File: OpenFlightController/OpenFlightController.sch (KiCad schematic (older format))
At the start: 0 parts

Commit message: EdgeCuts PCB 0.1v
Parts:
- added U1: STM32F405RGT6, Package_SO:MAX7456, symbol STM32F405RGT6:STM32F405RGT6
- added U2: MAX7456EUI+, Package_SO:MAX7456, symbol MAX7456EUI_:MAX7456EUI+
- added U?: MPU-6000, Sensor_Motion:InvenSense_QFN-24_4x4mm_P0.5mm, symbol Sensor_Motion:MPU-6000
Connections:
- new net: U1.18 (VSS), U1.63 (VSS)
- new net: U1.19 (VDD), U1.32 (VDD), U1.48 (VDD), U1.64 (VDD)
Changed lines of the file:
@@
 Comment4 ""
 $EndDescr
+$Comp
+L STM32F405RGT6:STM32F405RGT6 U1
+U 1 1 5E3B0E09
+P 2150 3150
+F 0 "U1" H 2150 5620 50  0000 C CNN
+F 1 "STM32F405RGT6" H 2150 5529 50  0000 C CNN
+F 2 "Package_SO:MAX7456" H 2150 3150 50  0001 L BNN
+F 3 "LTR" H 2150 3150 50  0001 L BNN
+F 4 "STMicroelectronics" H 2150 3150 50  0001 L BNN "Campo4"
+F 5 "IPC-7351B" H 2150 3150 50  0001 L BNN "Campo5"
+	1    2150 3150
+	1    0    0    -1
+$EndComp
+$Comp
+L MAX7456EUI_:MAX7456EUI+ U2
+U 1 1 5E3B414B
+P 7900 2600
+F 0 "U2" H 7900 3670 50  0000 C CNN
+F 1 "MAX7456EUI+" H 7900 3579 50  0000 C CNN
+F 2 "Package_SO:MAX7456" H 7900 2600 50  0001 L BNN
+F 3 "" H 7900 2600 50  0001 C CNN
+	1    7900 2600
+	1    0    0    -1
+$EndComp
+$Comp
+L Sensor_Motion:MPU-6000 U?
+U 1 1 5E3B576F
+P 6950 5200
+F 0 "U?" H 6950 6081 50  0000 C CNN
+F 1 "MPU-6000" H 6950 5990 50  0000 C CNN
+F 2 "Sensor_Motion:InvenSense_QFN-24_4x4mm_P0.5mm" H 6950 4400 50  0001 C CNN
+F 3 "https://store.invensense.com/datasheets/invensense/MPU-6050_DataSheet_V3%204.pdf" H 6950 5050 50  0001 C CNN
+	1    6950 5200
+	1    0    0    -1
+$EndComp
 $EndSCHEMATC

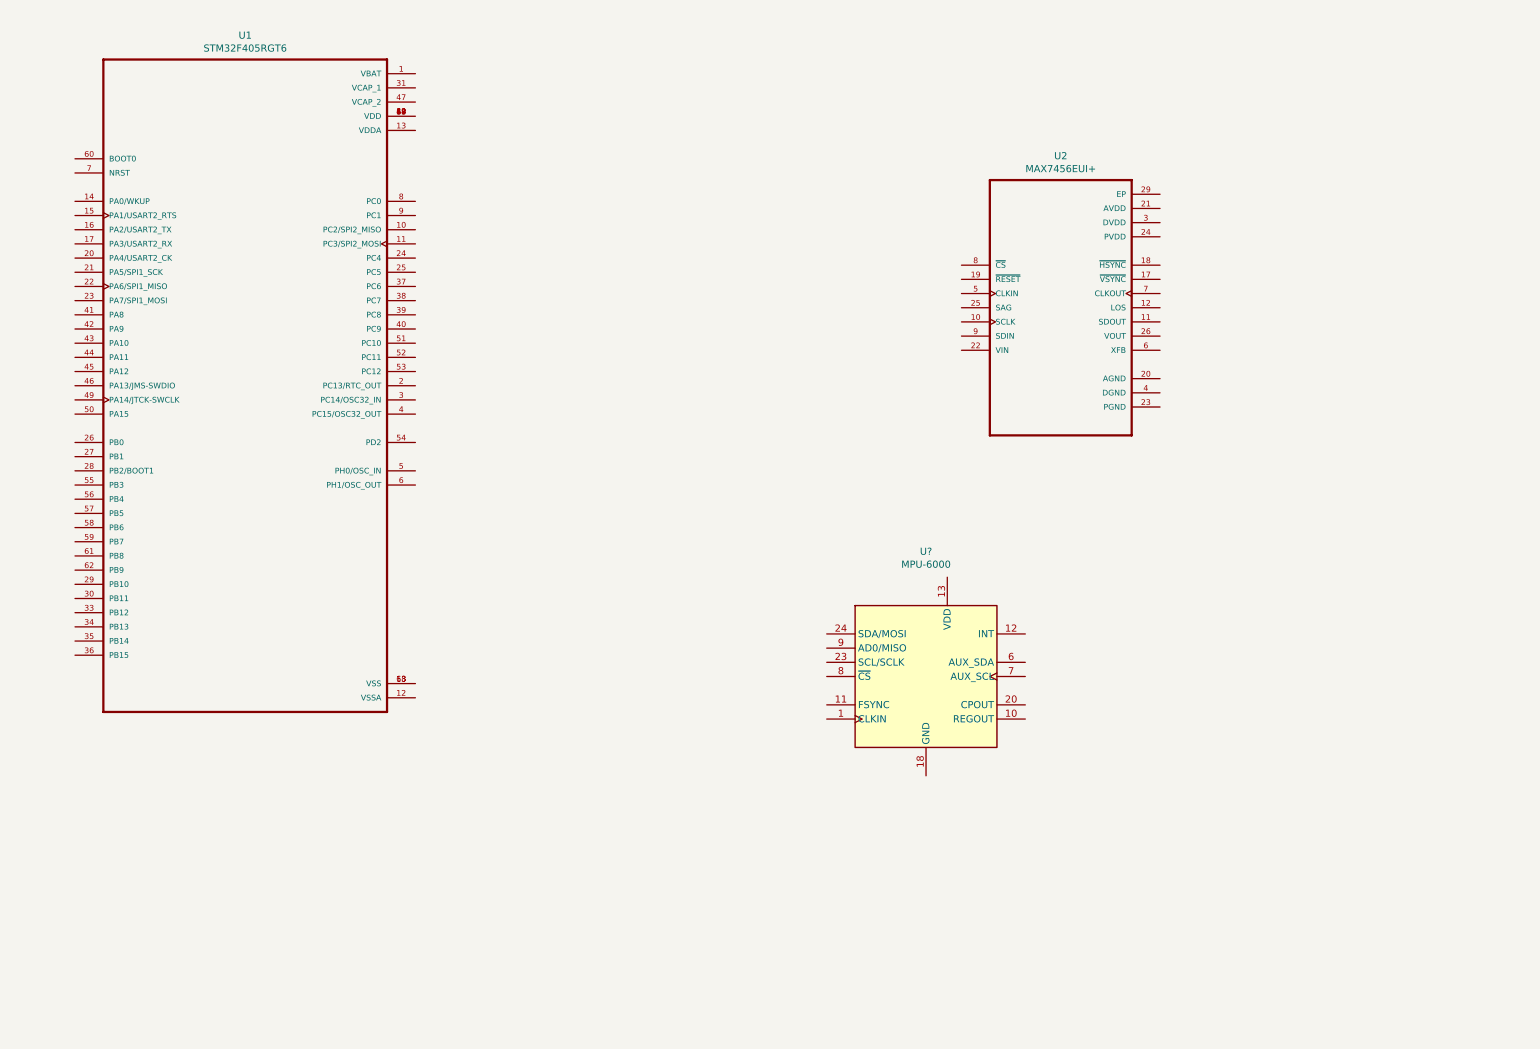
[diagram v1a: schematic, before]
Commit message: Add Power In 3v3
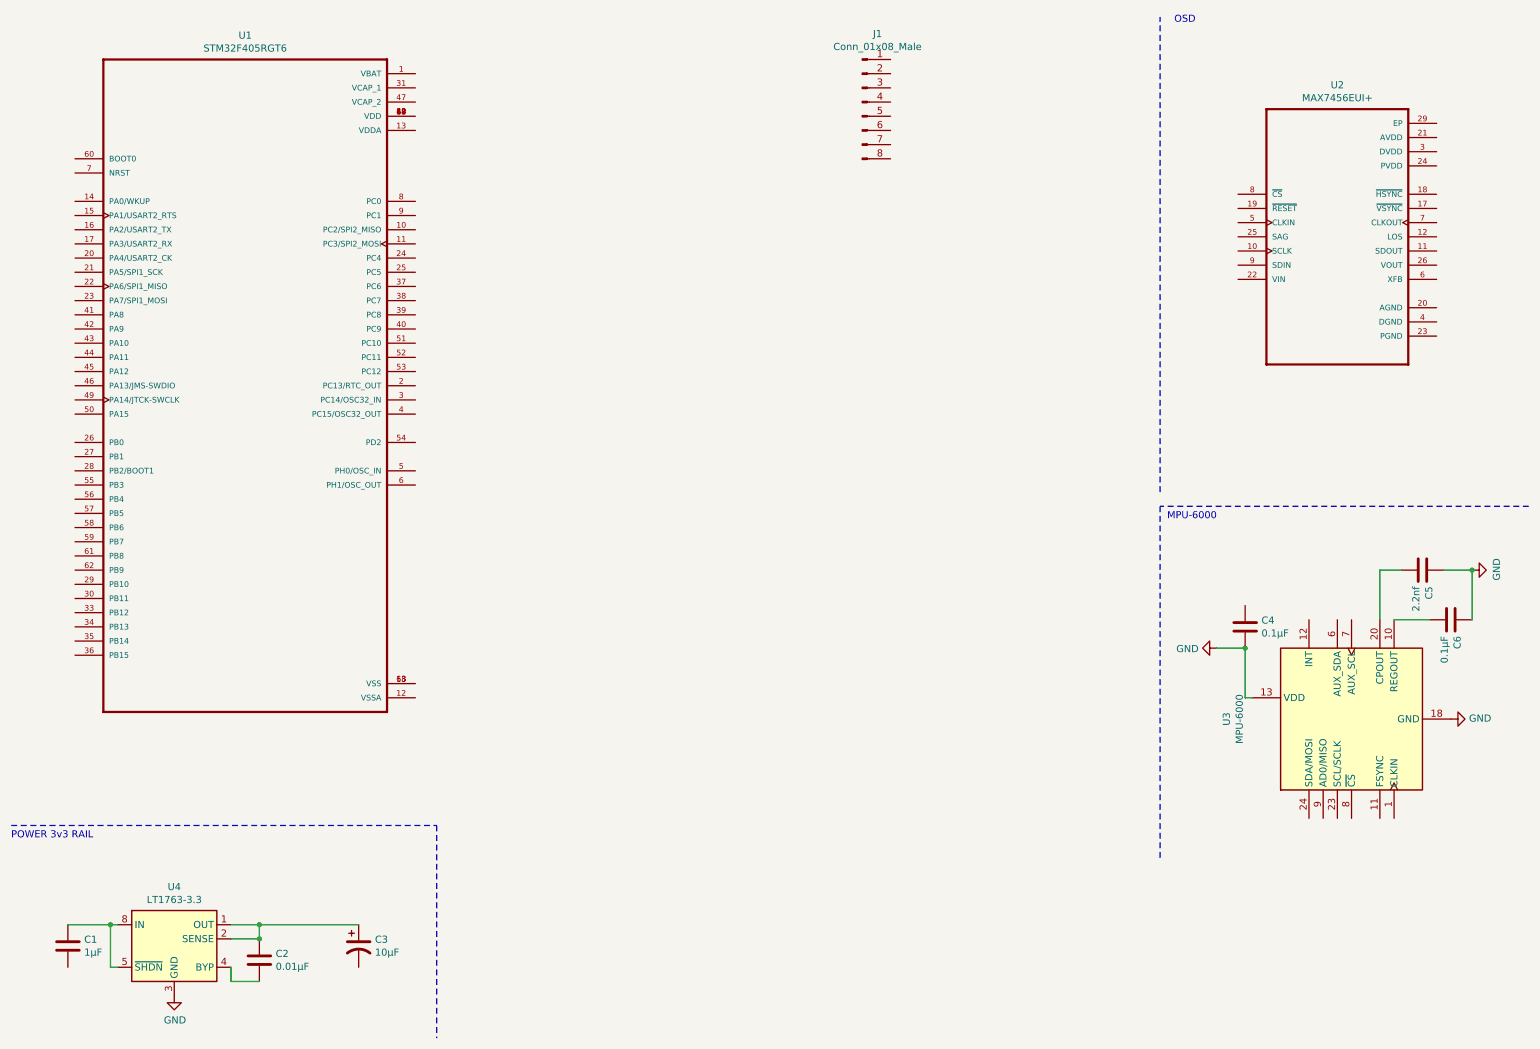
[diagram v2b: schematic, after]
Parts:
- added C1: 1µF, Capacitor_SMD:C_0603_1608Metric, symbol Device:C
- added C2: 0.01µF, Capacitor_SMD:C_0603_1608Metric, symbol Device:C
- added C3: 10µF, symbol Device:CP1
- added C4, C6: 0.1µF, Capacitor_SMD:C_0603_1608Metric, symbol Device:C
- added C5: 2.2nf, Capacitor_SMD:C_0603_1608Metric, symbol Device:C
- added J1: Conn_01x08_Male, Connector_JST:JST_GH_SM08B-GHS-TB_1x08-1MP_P1.25mm_Horizontal, symbol Connector:Conn_01x08_Male
- added U4: LT1763-3.3, Package_SO:SOP-8_3.76x4.96mm_P1.27mm, symbol Regulator_Linear:LT1763-3.3
- gave numbers to parts that had none: 1
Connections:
- net at U3.10 (REGOUT): now also C6.2
- net GND: now reaches U3.13 (VDD)
- net GND: now also U3.18 (GND), C4.2, C5.1, C6.1, U4.3 (GND)
- net at U3.20 (CPOUT): now also C5.2
- new net: C2.1, C3.1, U4.1 (OUT), U4.2 (SENSE)
- new net: C2.2, U4.4 (BYP)
- new net: C1.1, U4.5 (~SHDN), U4.8 (IN)
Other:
- note added: "MPU-6000\n"
- note added: "OSD"
- note added: "POWER 3v3 RAIL\n"
- moved on the sheet: U2, U3
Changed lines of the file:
@@
 L MAX7456EUI_:MAX7456EUI+ U2
 U 1 1 5E3B414B
-P 7900 2600
-F 0 "U2" H 7900 3670 50  0000 C CNN
-F 1 "MAX7456EUI+" H 7900 3579 50  0000 C CNN
-F 2 "Package_SO:MAX7456" H 7900 2600 50  0001 L BNN
-F 3 "" H 7900 2600 50  0001 C CNN
-	1    7900 2600
-	1    0    0    -1
-$EndComp
-$Comp
-L Sensor_Motion:MPU-6000 U?
+P 9850 2100
+F 0 "U2" H 9850 3170 50  0000 C CNN
+F 1 "MAX7456EUI+" H 9850 3079 50  0000 C CNN
+F 2 "Package_SO:MAX7456" H 9850 2100 50  0001 L BNN
+F 3 "" H 9850 2100 50  0001 C CNN
+	1    9850 2100
+	1    0    0    -1
+$EndComp
+$Comp
+L Regulator_Linear:LT1763-3.3 U4
+U 1 1 5E3E488E
+P 1650 7150
+F 0 "U4" H 1650 7617 50  0000 C CNN
+F 1 "LT1763-3.3" H 1650 7526 50  0000 C CNN
+F 2 "Package_SO:SOP-8_3.76x4.96mm_P1.27mm" H 1650 6800 50  0001 C CNN
+F 3 "https://www.analog.com/media/en/technical-documentation/data-sheets/1962fb.pdf" H 1650 6600 50  0001 C CNN
+	1    1650 7150
+	1    0    0    -1
+$EndComp
+$Comp
+L Device:C C2
+U 1 1 5E3E80B6
+P 2250 7200
+F 0 "C2" H 2365 7246 50  0000 L CNN
+F 1 "0.01µF" H 2365 7155 50  0000 L CNN
+F 2 "Capacitor_SMD:C_0603_1608Metric" H 2288 7050 50  0001 C CNN
+F 3 "~" H 2250 7200 50  0001 C CNN
+	1    2250 7200
+	1    0    0    -1
+$EndComp
+$Comp
+L Device:CP1 C3
+U 1 1 5E3E8CF6
+P 2950 7100
+F 0 "C3" H 3065 7146 50  0000 L CNN
+F 1 "10µF" H 3065 7055 50  0000 L CNN
+F 2 "" H 2950 7100 50  0001 C CNN
+F 3 "~" H 2950 7100 50  0001 C CNN
+	1    2950 7100
+	1    0    0    -1
+$EndComp
+$Comp
+L Device:C C1
+U 1 1 5E3E966D
+P 900 7100
+F 0 "C1" H 1015 7146 50  0000 L CNN
+F 1 "1µF" H 1015 7055 50  0000 L CNN
+F 2 "Capacitor_SMD:C_0603_1608Metric" H 938 6950 50  0001 C CNN
+F 3 "~" H 900 7100 50  0001 C CNN
+	1    900  7100
+	1    0    0    -1
+$EndComp
+Wire Wire Line
+	2050 7250 2050 7350
+Wire Wire Line
+	2050 7350 2250 7350
+Wire Wire Line
+	2250 7050 2250 6950
+Wire Wire Line
+	2250 6950 2050 6950
+Wire Wire Line
+	2050 7050 2250 7050
+Connection ~ 2250 7050
+Wire Wire Line
+	2250 6950 2950 6950
+Connection ~ 2250 6950
+Wire Wire Line
+	1250 7250 1200 7250
+Wire Wire Line
+	1200 7250 1200 6950
+Wire Wire Line
+	1200 6950 1250 6950
+Wire Wire Line
+	1200 6950 900  6950
+Connection ~ 1200 6950
+Wire Notes Line
+	500  6250 3500 6250
+Wire Notes Line
+	3500 6250 3500 7750
+Text Notes 500  6350 0    50   ~ 0
+POWER 3v3 RAIL\n
+$Comp
+L Device:C C5
+U 1 1 5E3EF61B
+P 10450 4450
+F 0 "C5" H 10565 4496 50  0000 L CNN
+F 1 "2.2nf" H 10565 4405 50  0000 L CNN
+F 2 "Capacitor_SMD:C_0603_1608Metric" H 10488 4300 50  0001 C CNN
+F 3 "~" H 10450 4450 50  0001 C CNN
+	1    10450 4450
+	0    1    1    0
+$EndComp
+$Comp
+L Device:C C6
+U 1 1 5E3F2D0D
+P 10650 4800
+F 0 "C6" H 10765 4846 50  0000 L CNN
+F 1 "0.1µF" H 10765 4755 50  0000 L CNN
+F 2 "Capacitor_SMD:C_0603_1608Metric" H 10688 4650 50  0001 C CNN
+F 3 "~" H 10650 4800 50  0001 C CNN
+	1    10650 4800
+	0    1    1    0
+$EndComp
+Wire Wire Line
+	9250 5350 9200 5350
+Wire Wire Line
+	9200 5350 9200 5000
+Wire Wire Line
+	9200 5000 9000 5000
+Connection ~ 9200 5000
+$Comp
+L Device:C C4
+U 1 1 5E3F0351
+P 9200 4850
+F 0 "C4" H 9315 4896 50  0000 L CNN
+F 1 "0.1µF" H 9315 4805 50  0000 L CNN
+F 2 "Capacitor_SMD:C_0603_1608Metric" H 9238 4700 50  0001 C CNN
+F 3 "~" H 9200 4850 50  0001 C CNN
+	1    9200 4850
+	1    0    0    -1
+$EndComp
+$Comp
+L Sensor_Motion:MPU-6000 U3
 U 1 1 5E3B576F
-P 6950 5200
-F 0 "U?" H 6950 6081 50  0000 C CNN
-F 1 "MPU-6000" H 6950 5990 50  0000 C CNN
-F 2 "Sensor_Motion:InvenSense_QFN-24_4x4mm_P0.5mm" H 6950 4400 50  0001 C CNN
-F 3 "https://store.invensense.com/datasheets/invensense/MPU-6050_DataSheet_V3%204.pdf" H 6950 5050 50  0001 C CNN
-	1    6950 5200
-	1    0    0    -1
-$EndComp
+P 9950 5500
+F 0 "U3" H 9950 6381 50  0000 C CNN
+F 1 "MPU-6000" H 9950 6290 50  0000 C CNN
+F 2 "Sensor_Motion:InvenSense_QFN-24_4x4mm_P0.5mm" H 9950 4700 50  0001 C CNN
+F 3 "https://store.invensense.com/datasheets/invensense/MPU-6050_DataSheet_V3%204.pdf" H 9950 5350 50  0001 C CNN
+	1    9950 5500
+	0    -1   -1   0
+$EndComp
+$Comp
+L power:GND #PWR0101
+U 1 1 5E4011D4
+P 10650 5500
+F 0 "#PWR0101" H 10650 5250 50  0001 C CNN
+F 1 "GND" V 10655 5372 50  0000 R CNN
+F 2 "" H 10650 5500 50  0001 C CNN
+F 3 "" H 10650 5500 50  0001 C CNN
+	1    10650 5500
+	0    -1   -1   0
+$EndComp
+$Comp
+L power:GND #PWR0102
+U 1 1 5E401C36
+P 10800 4450
+F 0 "#PWR0102" H 10800 4200 50  0001 C CNN
+F 1 "GND" H 10805 4277 50  0000 C CNN
+F 2 "" H 10800 4450 50  0001 C CNN
+F 3 "" H 10800 4450 50  0001 C CNN
+	1    10800 4450
+	0    -1   -1   0
+$EndComp
+$Comp
+L power:GND #PWR0103
+U 1 1 5E402469
+P 9000 5000
+F 0 "#PWR0103" H 9000 4750 50  0001 C CNN
+F 1 "GND" V 9005 4872 50  0000 R CNN
+F 2 "" H 9000 5000 50  0001 C CNN
+F 3 "" H 9000 5000 50  0001 C CNN
+	1    9000 5000
+	0    1    1    0
+$EndComp
+$Comp
+L power:GND #PWR0104
+U 1 1 5E402C2C
+P 1650 7450
+F 0 "#PWR0104" H 1650 7200 50  0001 C CNN
+F 1 "GND" H 1655 7277 50  0000 C CNN
+F 2 "" H 1650 7450 50  0001 C CNN
+F 3 "" H 1650 7450 50  0001 C CNN
+	1    1650 7450
+	1    0    0    -1
+$EndComp
+Wire Wire Line
+	10250 4800 10500 4800
+Wire Wire Line
+	10300 4450 10150 4450
+Wire Wire Line
+	10150 4450 10150 4800
+Wire Wire Line
+	10600 4450 10800 4450
+Connection ~ 10800 4450
+Wire Wire Line
+	10800 4450 10800 4800
+Wire Notes Line
+	11200 4000 8600 4000
+Wire Notes Line
+	8600 4000 8600 6500
+Text Notes 8650 4100 0    50   ~ 0
+MPU-6000\n
+Wire Notes Line
+	8600 3900 8600 550
+Text Notes 8700 600  0    50   ~ 0
+OSD
+$Comp
+L Connector:Conn_01x08_Male J1
+U 1 1 5E410CEA
+P 6500 1150
+F 0 "J1" H 6608 1631 50  0000 C CNN
+F 1 "Conn_01x08_Male" H 6608 1540 50  0000 C CNN
+F 2 "Connector_JST:JST_GH_SM08B-GHS-TB_1x08-1MP_P1.25mm_Horizontal" H 6500 1150 50  0001 C CNN
+F 3 "~" H 6500 1150 50  0001 C CNN
+	1    6500 1150
+	1    0    0    -1
+$EndComp
